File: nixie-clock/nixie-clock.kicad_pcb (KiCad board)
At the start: 2 copper layers, 294.1 x 50 mm, 76 parts, among them J1 Barrel_Jack, J2 Conn_01x02, J3 Conn_01x02, J4 Conn_01x01_MountingPin, J5 Conn_01x01_MountingPin, J6 Conn_01x01_MountingPin, J7 Conn_01x01_MountingPin, J8 Conn_01x01_MountingPin, Q1 2N7002, Q2 2N7002, Q3 2N7002, Q4 2N7002, Q5 2N7002, Q6 Q_Photo_NPN, Q7 PSMN014-80YL, T1 NA5920-AL, U1 ESP32-WROOM-32D, U2 HV5523, U3 HV5523, U4 TPS40210, U5 LDL1117, U6 DS3231M, U7 LDL1117

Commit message: Nixie Clock Fixes / Tweaks
- Connect TPS40210 power pad to ground.
- Exact board outlines
- Remove refs from mounting holes
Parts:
- moved G*** 1.20 mm to (349.1, 207.4)
- moved G*** 1.00 mm to (399.9, 207.4)
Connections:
- U4 pad 11: (no net) -> GND
- U6 pad 2: GND -> +3V3
- U6 pad 6: +3V3 -> GND
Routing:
- net +3V3: track 189.4 -> 185.0 mm
- net GND: track 50.0 -> 51.0 mm, vias 1318 -> 1322
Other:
- board size 294.1 x 50 mm -> 294 x 50 mm

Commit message: HV power supply works, swap tubes to other side of board
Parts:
- removed D1: D_Zener, Diode_SMD:D_SOD-123
- removed D2: D_Schottky, Diode_SMD:D_1206_3216Metric_Castellated
- Q6, R13, V1, V2, V3, V4, V5, V6: moved to B.Cu
- Q7: value PSMN014-80YL -> BUK7Y9R9-80EX
- moved Q4 4.19 mm to (273.5, 171.7)
- moved Q1 4.19 mm to (262.1, 171.6)
- moved Q2 4.19 mm to (269.7, 171.7)
- moved Q3 4.19 mm to (258.3, 171.6)
- moved Q5 4.19 mm to (265.9, 171.6)
- moved R1 4.19 mm to (262.1, 174.4)
- moved R2 4.19 mm to (269.7, 174.4)
- moved R3 4.19 mm to (258.3, 174.4)
- moved R4 4.19 mm to (273.5, 174.4)
- moved R5 4.19 mm to (265.9, 174.4)
- moved R23 1.99 mm to (403.4, 199.5)
- moved R21 1.72 mm to (323.4, 199.6)
- moved R18 1.49 mm to (208.4, 200.0)
- moved R22 1.18 mm to (368.4, 200.2)
- moved C19 1.05 mm to (268.2, 181.2)
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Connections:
- D3 pad 1: Net-(D3-Pad1) -> +170V
- D3 pad 2: +170V -> Net-(D3-Pad2)
- T1 pad 5: Net-(D3-Pad1) -> Net-(D3-Pad2)
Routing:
- net Net-(U2-Pad43): track 132.8 -> 98.8 mm
- net Net-(U3-Pad43): track 81.0 -> 49.9 mm
- net Net-(U2-Pad36): track 90.8 -> 60.0 mm
- net Net-(U3-Pad12): track 144.1 -> 114.1 mm
- net Net-(U2-Pad9): track 80.6 -> 51.6 mm
- net Net-(U2-Pad13): track 69.6 -> 42.6 mm
- net Net-(U2-Pad19): track 40.9 -> 14.1 mm
- net Net-(U2-Pad14): track 41.4 -> 15.4 mm
- net Net-(U3-Pad14): track 97.9 -> 71.9 mm
- net Net-(U3-Pad9): track 39.3 -> 13.7 mm
- net Net-(U2-Pad44): track 130.3 -> 104.7 mm
- net Net-(U2-Pad3): track 33.2 -> 57.8 mm
- net Net-(U3-Pad11): track 144.0 -> 119.6 mm
- net Net-(U2-Pad17): track 15.9 -> 39.9 mm
- net Net-(U3-Pad44): track 78.6 -> 56.4 mm
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- added copper zone on F.Cu, net Net-(D2-Pad2)
- removed copper zone on F.Cu, net Net-(D3-Pad1)
- removed copper zone on F.Cu, net Net-(Q7-Pad5)

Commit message: Tweak couple things before sending to fab
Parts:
- U2, U3: footprint Package_DFN_QFN:QFN-44-1EP_7x7mm_P0.5mm_EP5.15x5.15mm -> Package_DFN_QFN:QFN-44-1EP_7x7mm_P0.5mm_EP5.15x5.15mm_ThermalVias
- moved G*** 51.2 mm to (348.7, 206.3)
- moved G*** 44.2 mm to (304.9, 206.2)
- moved R10 24.4 mm to (426.0, 206.2), turned to 0 degrees
- moved R16 23.9 mm to (423.0, 205.3)
- moved R17 23.9 mm to (421.1, 205.3)
- moved C5 23.3 mm to (427.0, 203.3), turned to 90 degrees
- moved C6 22.5 mm to (425.0, 203.3), turned to 90 degrees
- moved C3 17.1 mm to (424.7, 199.6), turned to 270 degrees
- moved R6 16.8 mm to (425.2, 195.8), turned to 270 degrees
- moved C2 14.0 mm to (427.2, 195.8), turned to 90 degrees
- moved U4 12.1 mm to (429.1, 199.5), turned to 0 degrees
- moved Q7 10.2 mm to (437.3, 190.9), turned to 90 degrees
- moved C12 6.96 mm to (430.1, 196.7), turned to 180 degrees
- moved C10 6.41 mm to (430.1, 194.8), turned to 180 degrees
- moved C17 6.30 mm to (432.3, 182.3), turned to 90 degrees
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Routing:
- net +170V: track 250.8 -> 270.6 mm, vias 22 -> 21
- net GND: track 38.3 -> 52.2 mm, vias 514 -> 1165
- net Net-(C6-Pad1): track 0.00 -> 12.8 mm
- net +3V3: track 184.4 -> 177.4 mm
- net Net-(Q7-Pad4): track 0.00 -> 6.36 mm
- net Net-(R12-Pad2): track 2.23 -> 6.43 mm
- net Net-(D3-Pad2): track 0.00 -> 3.95 mm
- net Net-(C3-Pad1): track 5.91 -> 2.76 mm
- net Net-(Q7-Pad1): track 0.00 -> 2.36 mm
- net VDD: track 16.4 -> 18.5 mm
- net Net-(U2-Pad3): track 57.8 -> 59.8 mm
- net Net-(U2-Pad8): track 66.4 -> 64.5 mm
- net Net-(R19-Pad2): track 25.5 -> 23.6 mm
- net Net-(C5-Pad1): track 0.00 -> 1.87 mm
- net Net-(R20-Pad2): track 25.6 -> 23.7 mm
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- added copper zone on F.Cu, net Net-(Q7-Pad5)
- removed copper zone on F.Cu, net Net-(C11-Pad1)
- removed copper zone on F.Cu, net Net-(C2-Pad1)
- removed copper zone on F.Cu, net Net-(C5-Pad1)
- removed copper zone on F.Cu, net Net-(C5-Pad2)
- removed copper zone on F.Cu, net Net-(C6-Pad1)
- removed copper zone on F.Cu, net Net-(D1-Pad1)
- removed copper zone on F.Cu, net Net-(D2-Pad2)
- removed copper zone on F.Cu, net Net-(Q7-Pad4)

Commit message: Annotate remaining footprints
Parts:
- removed G***: LOGO, custom-parts:ProjectName125-800
- removed G***: LOGO, custom-parts:VersionString125-800
- removed the J3 at (175.2, 176.9)
- removed the Q1 at (262.1, 171.6)
- removed the Q2 at (269.7, 171.7)
- removed Q3, Q4, Q5: 2N7002, Package_TO_SOT_SMD:SOT-23
- removed the R1 at (262.1, 174.4)
- removed the R2 at (269.7, 174.4)
- removed the R3 at (258.3, 174.4)
- removed the R4 at (273.5, 174.4)
- removed the R5 at (265.9, 174.4)
- added C1: 100uF, Capacitor_SMD:C_0805_2012Metric_Pad1.15x1.40mm_HandSolder, F.Cu at (300.2, 129.2)
- added C16: 0.1uF, Capacitor_SMD:C_0805_2012Metric_Pad1.15x1.40mm_HandSolder, F.Cu at (272.1, 125.0)
- added C17: 0.1uF, Capacitor_SMD:C_0805_2012Metric_Pad1.15x1.40mm_HandSolder, F.Cu at (272.1, 126.9)
- added C18: 4.7uF, Capacitor_SMD:C_0805_2012Metric_Pad1.15x1.40mm_HandSolder, F.Cu at (275.8, 125.0)
- added C19: 0.1uF, Capacitor_SMD:C_0805_2012Metric_Pad1.15x1.40mm_HandSolder, F.Cu at (272.1, 128.9)
- added R12: 22.1K, Resistor_SMD:R_0805_2012Metric_Pad1.15x1.40mm_HandSolder, F.Cu at (279.6, 125.0)
- added R13: 47.5K, Resistor_SMD:R_0805_2012Metric_Pad1.15x1.40mm_HandSolder, F.Cu at (275.8, 128.9)
- added R14: 1K, Resistor_SMD:R_0805_2012Metric_Pad1.15x1.40mm_HandSolder, F.Cu at (279.6, 126.9)
- added R6: 10K, Resistor_SMD:R_0805_2012Metric_Pad1.15x1.40mm_HandSolder, F.Cu at (275.8, 126.9)
- added U4: DS3231M, Package_SO:SOIC-8_3.9x4.9mm_P1.27mm, F.Cu at (182.8, 203.8)
- added U7: CP2102N-A01-GQFN24, Package_DFN_QFN:QFN-24-1EP_4x4mm_P0.5mm_EP2.6x2.6mm, F.Cu at (309.6, 128.3)
- C2: renamed from C1; value 10uF -> 1uF
- J2: value Conn_01x02 -> USB_B_Mini; footprint Connector_PinHeader_1.00mm:PinHeader_1x02_P1.00mm_Vertical -> custom-parts:54819-0589
- R17: renamed from R18; value 3.3k -> 7.3k
- R18: renamed from R19; value 3.3k -> 7.3k
- R19: renamed from R20; value 3.3k -> 7.3k
- R20: renamed from R21; value 3.3k -> 7.3k
- R21: renamed from R22; value 3.3k -> 7.3k
- R22: renamed from R23; value 3.3k -> 7.3k
- U6: value DS3231M -> TXB0108PWR; footprint Package_SO:SO-8_5.3x6.2mm_P1.27mm -> Package_SO:TSSOP-20_4.4x6.5mm_P0.65mm
- moved U6 152.0 mm to (311.0, 122.1)
- moved J2 126.0 mm to (300.9, 123.4), turned to 0 degrees
- renumbered C9 to C10, C10 to C11, C11 to C12, C12 to C13, C13 to C14, C14 to C15, C15 to C20, C16 to C21, C17 to C22, C18 to C23, C19 to C24, C2 to C3, C3 to C4, C4 to C5, C5 to C6, C6 to C7, C7 to C8, C8 to C9, D3 to D1, J4 to J3, J5 to J4, J6 to J5, J7 to J6, J8 to J7, Q6 to Q1, Q7 to Q2, R6 to R1, R14 to R10, R15 to R11, R16 to R15, R17 to R16, R7 to R2, R8 to R3, R9 to R4, R10 to R5, R11 to R7, R12 to R8, R13 to R9, U4 to U2, U5 to U3, U7 to U5, U2 to U8, U3 to U9
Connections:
- net Net-(R7-Pad2) renamed /ESP_EN
- J2 pad 1: GND -> Net-(J2-Pad1)
- T1 pad 6: Net-(T1-Pad6) -> (no net)
- T1 pad 7: Net-(T1-Pad7) -> (no net)
- U1 pad 14: Net-(U1-Pad14) -> (no net)
- U1 pad 17: Net-(U1-Pad17) -> (no net)
- U1 pad 18: Net-(U1-Pad18) -> (no net)
- U1 pad 19: Net-(U1-Pad19) -> (no net)
- U1 pad 20: Net-(U1-Pad20) -> (no net)
- U1 pad 21: Net-(U1-Pad21) -> (no net)
- U1 pad 22: Net-(U1-Pad22) -> (no net)
- U1 pad 24: Net-(U1-Pad24) -> (no net)
- U1 pad 25: Net-(J2-Pad2) -> /BOOT_MODE
- U1 pad 26: Net-(U1-Pad26) -> (no net)
- U1 pad 29: Net-(U1-Pad29) -> (no net)
- U1 pad 31: Net-(U1-Pad31) -> (no net)
- U1 pad 32: Net-(U1-Pad32) -> (no net)
- U1 pad 33: Net-(U1-Pad33) -> (no net)
- U1 pad 34: Net-(J3-Pad2) -> /RX
- U1 pad 35: Net-(J3-Pad1) -> /TX
- U1 pad 36: Net-(U1-Pad36) -> (no net)
- U1 pad 37: Net-(U1-Pad37) -> (no net)
- U1 pad 4: Net-(U1-Pad4) -> (no net)
- U1 pad 5: Net-(U1-Pad5) -> (no net)
- U1 pad 6: Net-(U1-Pad6) -> (no net)
- U1 pad 7: Net-(U1-Pad7) -> (no net)
- U6 pad 1: Net-(U6-Pad1) -> /MOSI
- U6 pad 3: /RTC_INT -> /SCLK
- U6 pad 4: /RTC_RST -> /LE
- U6 pad 5: GND -> /POL
- U6 pad 6: GND -> /BL
- U6 pad 7: /RTC_SDA -> (no net)
- U6 pad 8: /RTC_SCL -> (no net)
- U8 pad 1: Net-(U2-Pad1) -> Net-(U8-Pad1)
- U8 pad 10: Net-(U2-Pad10) -> Net-(U8-Pad10)
- U8 pad 11: Net-(U2-Pad11) -> Net-(U8-Pad11)
- U8 pad 12: Net-(U2-Pad12) -> Net-(U8-Pad12)
- U8 pad 13: Net-(U2-Pad13) -> Net-(U8-Pad13)
- U8 pad 14: Net-(U2-Pad14) -> Net-(U8-Pad14)
- U8 pad 15: Net-(U2-Pad15) -> Net-(U8-Pad15)
- U8 pad 16: Net-(U2-Pad16) -> Net-(U8-Pad16)
- U8 pad 17: Net-(U2-Pad17) -> Net-(U8-Pad17)
- U8 pad 18: Net-(U2-Pad18) -> Net-(U8-Pad18)
- U8 pad 19: Net-(U2-Pad19) -> Net-(U8-Pad19)
- U8 pad 2: Net-(U2-Pad2) -> Net-(U8-Pad2)
- U8 pad 20: Net-(U2-Pad20) -> Net-(U8-Pad20)
- U8 pad 21: Net-(U2-Pad21) -> (no net)
- U8 pad 22: Net-(U2-Pad22) -> (no net)
- U8 pad 24: Net-(U2-Pad24) -> (no net)
- U8 pad 25: Net-(U2-Pad25) -> (no net)
- U8 pad 26: Net-(U2-Pad26) -> (no net)
- U8 pad 27: Net-(Q4-Pad3) -> Net-(U6-Pad16)
- U8 pad 28: Net-(Q2-Pad3) -> Net-(U6-Pad18)
- U8 pad 3: Net-(U2-Pad3) -> Net-(U8-Pad3)
- U8 pad 31: Net-(Q5-Pad3) -> Net-(U6-Pad17)
- U8 pad 32: Net-(Q1-Pad3) -> Net-(U6-Pad20)
- U8 pad 33: Net-(Q3-Pad3) -> Net-(U6-Pad15)
- U8 pad 34: Net-(U2-Pad34) -> (no net)
- U8 pad 35: Net-(U2-Pad35) -> Net-(U8-Pad35)
- U8 pad 36: Net-(U2-Pad36) -> Net-(U8-Pad36)
- U8 pad 37: Net-(U2-Pad37) -> Net-(U8-Pad37)
- U8 pad 38: Net-(U2-Pad38) -> Net-(U8-Pad38)
- U8 pad 39: Net-(U2-Pad39) -> Net-(U8-Pad39)
- U8 pad 4: Net-(U2-Pad4) -> Net-(U8-Pad4)
- U8 pad 40: Net-(U2-Pad40) -> Net-(U8-Pad40)
- U8 pad 41: Net-(U2-Pad41) -> Net-(U8-Pad41)
- U8 pad 42: Net-(U2-Pad42) -> Net-(U8-Pad42)
- U8 pad 43: Net-(U2-Pad43) -> Net-(U8-Pad43)
- U8 pad 44: Net-(U2-Pad44) -> Net-(U8-Pad44)
- U8 pad 5: Net-(U2-Pad5) -> Net-(U8-Pad5)
- U8 pad 6: Net-(U2-Pad6) -> Net-(U8-Pad6)
- U8 pad 7: Net-(U2-Pad7) -> Net-(U8-Pad7)
- U8 pad 8: Net-(U2-Pad8) -> Net-(U8-Pad8)
- U8 pad 9: Net-(U2-Pad9) -> Net-(U8-Pad9)
- U9 pad 1: Net-(U3-Pad1) -> Net-(U9-Pad1)
- U9 pad 10: Net-(U3-Pad10) -> Net-(U9-Pad10)
- U9 pad 11: Net-(U3-Pad11) -> Net-(U9-Pad11)
- U9 pad 12: Net-(U3-Pad12) -> Net-(U9-Pad12)
- U9 pad 13: Net-(U3-Pad13) -> Net-(U9-Pad13)
- U9 pad 14: Net-(U3-Pad14) -> Net-(U9-Pad14)
- U9 pad 15: Net-(U3-Pad15) -> Net-(U9-Pad15)
- U9 pad 16: Net-(U3-Pad16) -> Net-(U9-Pad16)
- U9 pad 17: Net-(U3-Pad17) -> Net-(U9-Pad17)
- U9 pad 18: Net-(U3-Pad18) -> Net-(U9-Pad18)
- U9 pad 19: Net-(U3-Pad19) -> Net-(U9-Pad19)
- U9 pad 2: Net-(U3-Pad2) -> Net-(U9-Pad2)
- U9 pad 20: Net-(U3-Pad20) -> Net-(U9-Pad20)
- U9 pad 21: Net-(U3-Pad21) -> (no net)
- U9 pad 22: Net-(U3-Pad22) -> (no net)
- U9 pad 23: Net-(U3-Pad23) -> (no net)
- U9 pad 24: Net-(U3-Pad24) -> (no net)
- U9 pad 25: Net-(U3-Pad25) -> (no net)
- U9 pad 26: Net-(U3-Pad26) -> (no net)
- U9 pad 27: Net-(Q4-Pad3) -> Net-(U6-Pad16)
- U9 pad 28: Net-(Q2-Pad3) -> Net-(U6-Pad18)
- U9 pad 3: Net-(U3-Pad3) -> Net-(U9-Pad3)
- U9 pad 31: Net-(Q5-Pad3) -> Net-(U6-Pad17)
- U9 pad 33: Net-(Q3-Pad3) -> Net-(U6-Pad15)
- U9 pad 34: Net-(U3-Pad34) -> (no net)
- U9 pad 35: Net-(U3-Pad35) -> Net-(U9-Pad35)
- U9 pad 36: Net-(U3-Pad36) -> Net-(U9-Pad36)
- U9 pad 37: Net-(U3-Pad37) -> Net-(U9-Pad37)
- U9 pad 38: Net-(U3-Pad38) -> Net-(U9-Pad38)
- U9 pad 39: Net-(U3-Pad39) -> Net-(U9-Pad39)
- U9 pad 4: Net-(U3-Pad4) -> Net-(U9-Pad4)
- U9 pad 40: Net-(U3-Pad40) -> Net-(U9-Pad40)
- U9 pad 41: Net-(U3-Pad41) -> Net-(U9-Pad41)
- U9 pad 42: Net-(U3-Pad42) -> Net-(U9-Pad42)
- U9 pad 43: Net-(U3-Pad43) -> Net-(U9-Pad43)
- U9 pad 44: Net-(U3-Pad44) -> Net-(U9-Pad44)
- U9 pad 5: Net-(U3-Pad5) -> Net-(U9-Pad5)
- U9 pad 6: Net-(U3-Pad6) -> Net-(U9-Pad6)
- U9 pad 7: Net-(U3-Pad7) -> Net-(U9-Pad7)
- U9 pad 8: Net-(U3-Pad8) -> Net-(U9-Pad8)
- U9 pad 9: Net-(U3-Pad9) -> Net-(U9-Pad9)
- V1 pad 1: Net-(V1-Pad1) -> (no net)
- V1 pad 10: Net-(U2-Pad36) -> Net-(U8-Pad37)
- V1 pad 11: Net-(U2-Pad35) -> Net-(U8-Pad36)
- V1 pad 13: Net-(U2-Pad44) -> Net-(U8-Pad35)
- V1 pad 14: Net-(U2-Pad43) -> Net-(U8-Pad44)
- V1 pad 2: Net-(U2-Pad38) -> Net-(U8-Pad39)
- V1 pad 3: Net-(U2-Pad39) -> Net-(U8-Pad40)
- V1 pad 5: Net-(U2-Pad40) -> Net-(U8-Pad41)
- V1 pad 6: Net-(U2-Pad41) -> Net-(U8-Pad42)
- V1 pad 7: Net-(U2-Pad37) -> Net-(U8-Pad38)
- V1 pad 8: Net-(V1-Pad8) -> (no net)
- V1 pad 9: Net-(U2-Pad42) -> Net-(U8-Pad43)
- V2 pad 1: Net-(V2-Pad1) -> (no net)
- V2 pad 10: Net-(U2-Pad2) -> Net-(U8-Pad3)
- V2 pad 11: Net-(U2-Pad1) -> Net-(U8-Pad2)
- V2 pad 13: Net-(U2-Pad10) -> Net-(U8-Pad1)
- V2 pad 14: Net-(U2-Pad9) -> Net-(U8-Pad10)
- V2 pad 2: Net-(U2-Pad4) -> Net-(U8-Pad5)
- V2 pad 3: Net-(U2-Pad5) -> Net-(U8-Pad6)
- V2 pad 5: Net-(U2-Pad6) -> Net-(U8-Pad7)
- V2 pad 6: Net-(U2-Pad7) -> Net-(U8-Pad8)
- V2 pad 7: Net-(U2-Pad3) -> Net-(U8-Pad4)
- V2 pad 8: Net-(V2-Pad8) -> (no net)
- V2 pad 9: Net-(U2-Pad8) -> Net-(U8-Pad9)
- V3 pad 1: Net-(V3-Pad1) -> (no net)
- V3 pad 10: Net-(U2-Pad12) -> Net-(U8-Pad13)
- V3 pad 11: Net-(U2-Pad11) -> Net-(U8-Pad12)
- V3 pad 13: Net-(U2-Pad20) -> Net-(U8-Pad11)
- V3 pad 14: Net-(U2-Pad19) -> Net-(U8-Pad20)
- V3 pad 2: Net-(U2-Pad14) -> Net-(U8-Pad15)
- V3 pad 3: Net-(U2-Pad15) -> Net-(U8-Pad16)
- V3 pad 5: Net-(U2-Pad16) -> Net-(U8-Pad17)
- V3 pad 6: Net-(U2-Pad17) -> Net-(U8-Pad18)
- V3 pad 7: Net-(U2-Pad13) -> Net-(U8-Pad14)
- V3 pad 8: Net-(V3-Pad8) -> (no net)
- V3 pad 9: Net-(U2-Pad18) -> Net-(U8-Pad19)
- V4 pad 1: Net-(V4-Pad1) -> (no net)
- V4 pad 10: Net-(U3-Pad36) -> Net-(U9-Pad37)
- V4 pad 11: Net-(U3-Pad35) -> Net-(U9-Pad36)
- V4 pad 13: Net-(U3-Pad44) -> Net-(U9-Pad35)
- V4 pad 14: Net-(U3-Pad43) -> Net-(U9-Pad44)
- V4 pad 2: Net-(U3-Pad38) -> Net-(U9-Pad39)
- V4 pad 3: Net-(U3-Pad39) -> Net-(U9-Pad40)
- V4 pad 5: Net-(U3-Pad40) -> Net-(U9-Pad41)
- V4 pad 6: Net-(U3-Pad41) -> Net-(U9-Pad42)
- V4 pad 7: Net-(U3-Pad37) -> Net-(U9-Pad38)
- V4 pad 8: Net-(V4-Pad8) -> (no net)
- V4 pad 9: Net-(U3-Pad42) -> Net-(U9-Pad43)
- V5 pad 1: Net-(V5-Pad1) -> (no net)
- V5 pad 10: Net-(U3-Pad2) -> Net-(U9-Pad3)
- V5 pad 11: Net-(U3-Pad1) -> Net-(U9-Pad2)
- V5 pad 13: Net-(U3-Pad10) -> Net-(U9-Pad1)
- V5 pad 14: Net-(U3-Pad9) -> Net-(U9-Pad10)
- V5 pad 2: Net-(U3-Pad4) -> Net-(U9-Pad5)
- V5 pad 3: Net-(U3-Pad5) -> Net-(U9-Pad6)
- V5 pad 5: Net-(U3-Pad6) -> Net-(U9-Pad7)
- V5 pad 6: Net-(U3-Pad7) -> Net-(U9-Pad8)
- V5 pad 7: Net-(U3-Pad3) -> Net-(U9-Pad4)
- V5 pad 8: Net-(V5-Pad8) -> (no net)
- V5 pad 9: Net-(U3-Pad8) -> Net-(U9-Pad9)
- V6 pad 1: Net-(V6-Pad1) -> (no net)
- V6 pad 10: Net-(U3-Pad12) -> Net-(U9-Pad13)
- V6 pad 11: Net-(U3-Pad11) -> Net-(U9-Pad12)
- V6 pad 13: Net-(U3-Pad20) -> Net-(U9-Pad11)
- V6 pad 14: Net-(U3-Pad19) -> Net-(U9-Pad20)
- V6 pad 2: Net-(U3-Pad14) -> Net-(U9-Pad15)
- V6 pad 3: Net-(U3-Pad15) -> Net-(U9-Pad16)
- V6 pad 5: Net-(U3-Pad16) -> Net-(U9-Pad17)
- V6 pad 6: Net-(U3-Pad17) -> Net-(U9-Pad18)
- V6 pad 7: Net-(U3-Pad13) -> Net-(U9-Pad14)
- V6 pad 8: Net-(V6-Pad8) -> (no net)
- V6 pad 9: Net-(U3-Pad18) -> Net-(U9-Pad19)
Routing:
- net Net-(U6-Pad15): track 0.00 -> 109.4 mm, vias 0 -> 4
- net Net-(Q3-Pad3): track 109.4 -> 0.00 mm, vias 4 -> 0
- net Net-(U6-Pad16): track 0.00 -> 101.6 mm, vias 0 -> 2
- net Net-(Q4-Pad3): track 101.6 -> 0.00 mm, vias 2 -> 0
- net Net-(U6-Pad18): track 0.00 -> 98.8 mm, vias 0 -> 2
- net Net-(Q2-Pad3): track 98.8 -> 0.00 mm, vias 2 -> 0
- net Net-(U6-Pad17): track 0.00 -> 98.6 mm, vias 0 -> 2
- net Net-(Q5-Pad3): track 98.6 -> 0.00 mm, vias 2 -> 0
- net Net-(U6-Pad20): track 0.00 -> 13.3 mm
- net Net-(Q1-Pad3): track 13.3 -> 0.00 mm
- net Net-(J2-Pad2): track 2.47 -> 0.00 mm
- net /BOOT_MODE: track 0.00 -> 2.47 mm
- net Net-(J3-Pad2): track 2.45 -> 0.00 mm
- net /RX: track 0.00 -> 2.45 mm
- net Net-(J3-Pad1): track 2.45 -> 0.00 mm
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
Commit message: Reroute everything affected by v1.1 changes
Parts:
- C1: footprint Capacitor_SMD:C_0805_2012Metric_Pad1.15x1.40mm_HandSolder -> Capacitor_SMD:C_1206_3216Metric_Pad1.42x1.75mm_HandSolder
- moved C1 148.6 mm to (171.4, 203.3), turned to 180 degrees
- moved U7 138.7 mm to (177.9, 171.4), turned to 180 degrees
- moved J2 119.8 mm to (188.8, 165.4), turned to 270 degrees
- moved U6 115.4 mm to (204.8, 167.4)
- moved R12 114.5 mm to (173.8, 168.7), turned to 270 degrees
- moved R13 111.4 mm to (171.8, 168.7), turned to 90 degrees
- moved R14 110.3 mm to (176.7, 166.8), turned to 270 degrees
- moved R6 106.3 mm to (181.5, 175.9), turned to 90 degrees
- moved C18 102.7 mm to (181.9, 166.7), turned to 45 degrees
- moved C17 99.2 mm to (180.5, 165.3), turned to 45 degrees
- moved C16 84.0 mm to (199.8, 167.8), turned to 90 degrees
- moved C20 81.2 mm to (299.2, 199.0)
- moved C5 81.2 mm to (308.6, 198.9)
- moved U5 81.2 mm to (303.9, 196.9)
- moved C19 77.7 mm to (207.4, 171.9), turned to 180 degrees
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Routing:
- net Net-(U3-Pad11): track 118.9 -> 0.00 mm
- net Net-(U2-Pad42): track 113.2 -> 0.00 mm
- net +3V3: track 177.4 -> 290.5 mm, vias 1 -> 16
- net Net-(U3-Pad12): track 113.1 -> 0.00 mm
- net Net-(U9-Pad20): track 0.00 -> 108.8 mm
- net Net-(U2-Pad44): track 104.7 -> 0.00 mm
- net Net-(U2-Pad41): track 104.5 -> 0.00 mm
- net Net-(U2-Pad43): track 98.8 -> 0.00 mm
- net Net-(U3-Pad13): track 98.0 -> 0.00 mm
- net Net-(U8-Pad37): track 0.00 -> 97.7 mm
- net Net-(U8-Pad36): track 0.00 -> 96.2 mm
- net Net-(U2-Pad40): track 94.7 -> 0.00 mm
- net Net-(U8-Pad38): track 0.00 -> 92.2 mm
- net Net-(U8-Pad35): track 0.00 -> 92.1 mm
- net Net-(U8-Pad44): track 0.00 -> 90.3 mm
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- added copper zone on F.Cu, net +3V3

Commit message: Fix logo and version
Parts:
- added G***: LOGO, custom-parts:ProjectName125-800, F.Cu at (0.00, 100.0)
- added G***: LOGO, custom-parts:ProjectName125-800, F.Cu at (304.9, 205.4)
- added G***: LOGO, custom-parts:VersionString125-800, F.Cu at (349.9, 205.4)

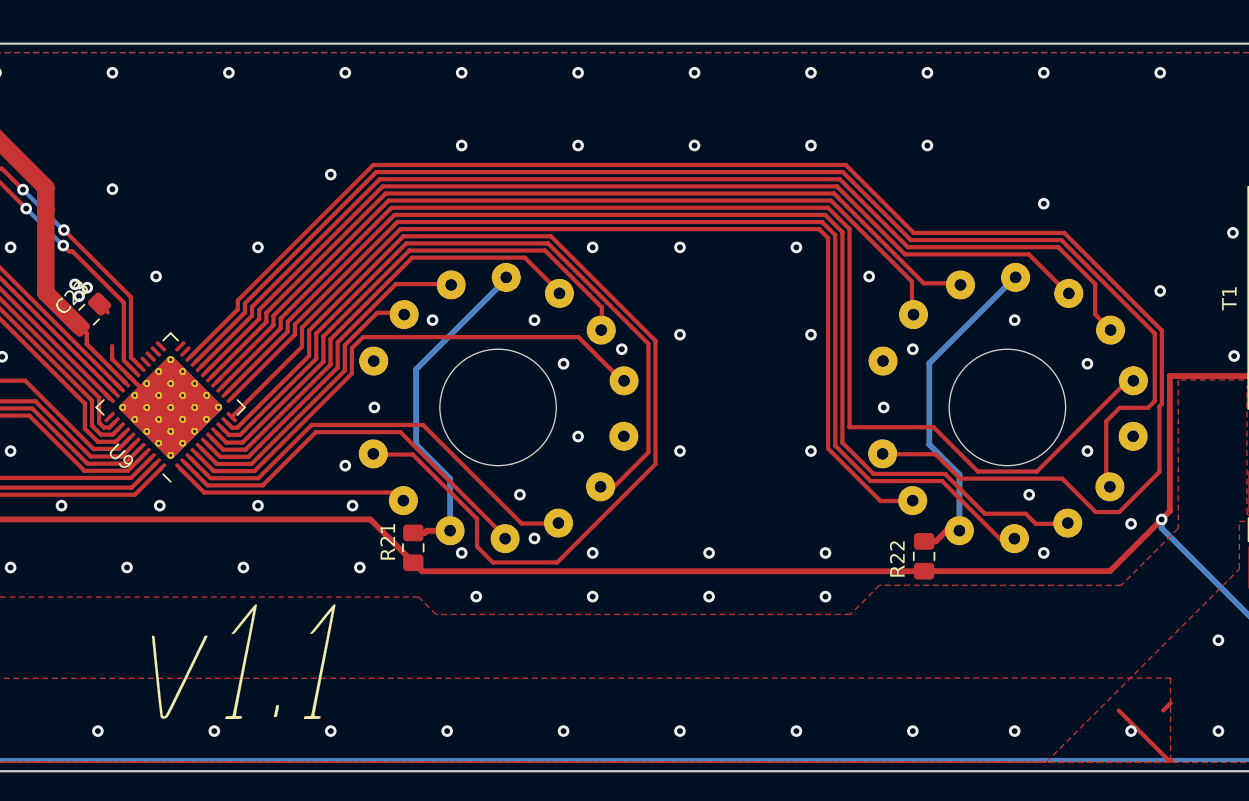
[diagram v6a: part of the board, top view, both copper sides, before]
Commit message: Add high voltage danger warnings
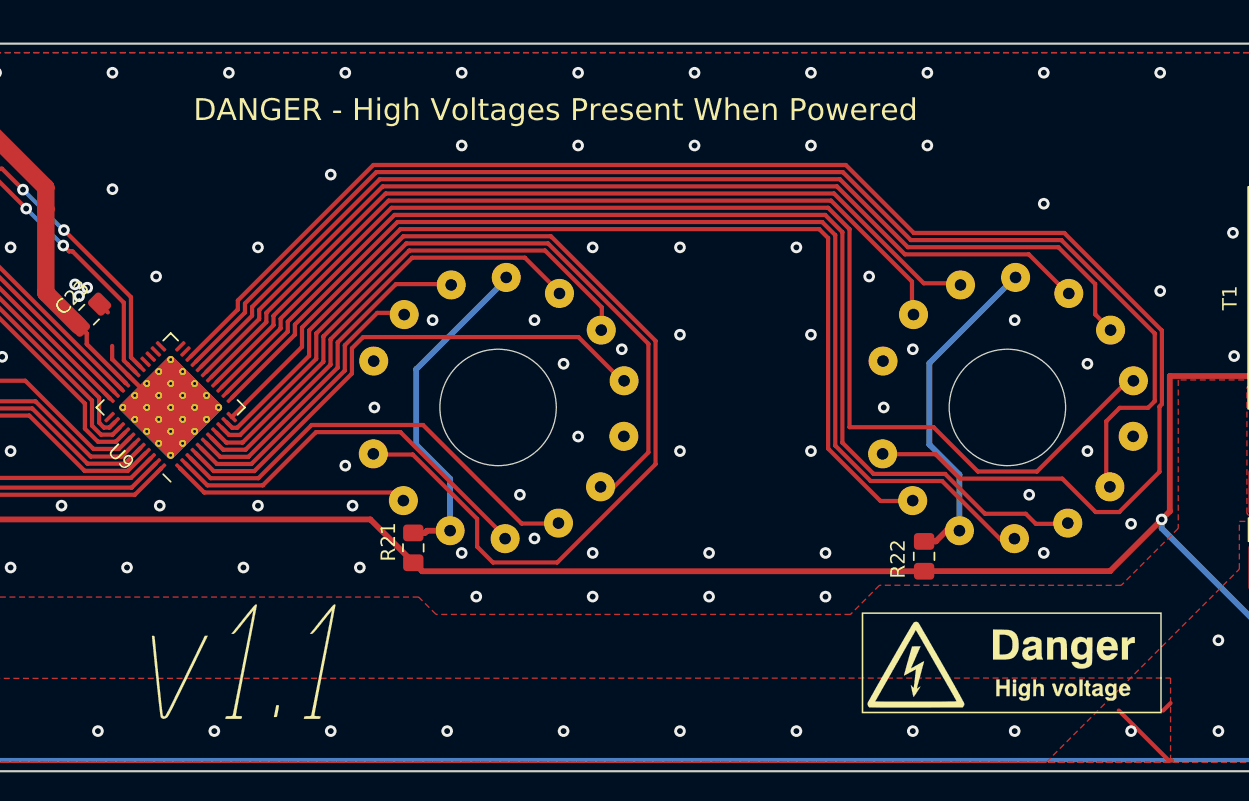
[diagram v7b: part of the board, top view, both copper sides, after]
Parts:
- added G***: LOGO, custom-parts:HVDangerSymbol, B.Cu at (224.6, 168.1)
- added G***: LOGO, custom-parts:HVDangerSymbol, F.Cu at (402.7, 205.4)
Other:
- board text added: "DANGER - High Voltages Present When Powered"

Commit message: Fix footprint in schematic
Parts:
- removed the G*** at (0.00, 100.0)
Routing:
- net (no net): track 0.88 -> 0.00 mm
